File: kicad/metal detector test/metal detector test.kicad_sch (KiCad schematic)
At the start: 102 parts, among them J1 3.5mm audio jack TRS, Q1 PNP, Q2 NPN, SW0 SW_SPST, SW1 SW_SPST, SW10 SW_SPST, SW2 SW_SPST, SW3 SW_SPST, SW4 SW_SPST, SW5 SW_SPST, SW6 SW_SPST, SW7 SW_SPST, SW8 SW_SPST, U1 op amp (higher voltage), U10 3.3v lin reg, U11 lp filter, U12 op amp (lower voltage), U2 nucleo-32 uC module, U3 9v lin reg, U4 5v lin reg, U5 3.3v lin reg, U6 audio amp, U7 lp filter, U8 switch debounce, U9 5v lin reg

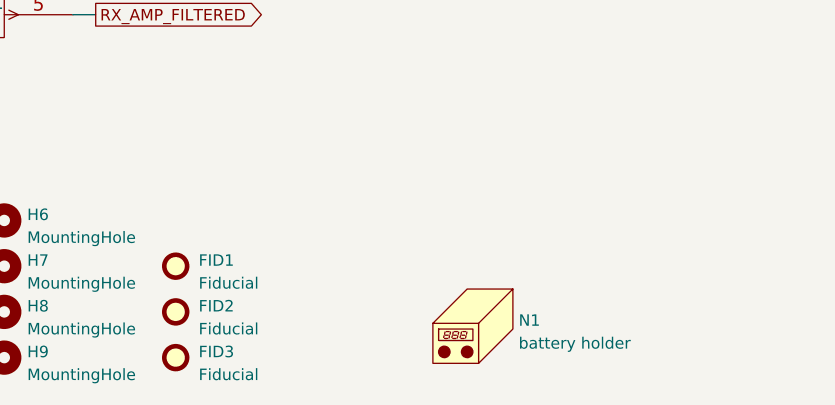
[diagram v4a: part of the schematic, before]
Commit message: Added a lot of fun silkscreen logos, and some other small tweaks
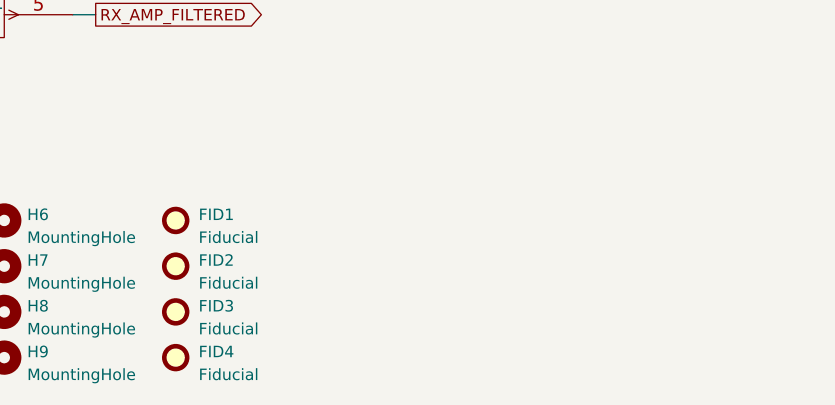
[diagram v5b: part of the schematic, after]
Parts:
- removed N1: battery holder, allen footprints:106990288_18650_x3_battery_holder, symbol Mechanical:Housing
- added FID4: Fiducial, Fiducial:Fiducial_0.5mm_Mask1.5mm, symbol Mechanical:Fiducial
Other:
- moved on the sheet: FID1, FID2, FID3
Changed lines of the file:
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@@
     )
   )
-  (symbol (lib_id "Mechanical:Fiducial") (at 124.46 194.31 0) (unit 1)
+  (symbol (lib_id "Mechanical:Fiducial") (at 124.46 189.23 0) (unit 1)
     (in_bom yes) (on_board yes) (dnp no) (fields_autoplaced)
-    (property "Reference" "FID3" (at 127 193.675 0)
+    (property "Reference" "FID3" (at 127 188.595 0)
       (effects (font (size 1.27 1.27)) (justify left))
     )
-    (property "Value" "Fiducial" (at 127 196.215 0)
+    (property "Value" "Fiducial" (at 127 191.135 0)
       (effects (font (size 1.27 1.27)) (justify left))
     )
-    (property "Footprint" "Fiducial:Fiducial_0.5mm_Mask1.5mm" (at 124.46 194.31 0)
+    (property "Footprint" "Fiducial:Fiducial_0.5mm_Mask1.5mm" (at 124.46 189.23 0)
       (effects (font (size 1.27 1.27)) hide)
     )
-    (property "Datasheet" "~" (at 124.46 194.31 0)
+    (property "Datasheet" "~" (at 124.46 189.23 0)
       (effects (font (size 1.27 1.27)) hide)
     )
-    (property "MPN" "" (at 124.46 194.31 0)
+    (property "MPN" "" (at 124.46 189.23 0)
       (effects (font (size 1.27 1.27)) hide)
     )
@@
     )
   )
-  (symbol (lib_id "Mechanical:Fiducial") (at 124.46 189.23 0) (unit 1)
+  (symbol (lib_id "Mechanical:Fiducial") (at 124.46 184.15 0) (unit 1)
     (in_bom yes) (on_board yes) (dnp no) (fields_autoplaced)
-    (property "Reference" "FID2" (at 127 188.595 0)
+    (property "Reference" "FID2" (at 127 183.515 0)
       (effects (font (size 1.27 1.27)) (justify left))
     )
-    (property "Value" "Fiducial" (at 127 191.135 0)
+    (property "Value" "Fiducial" (at 127 186.055 0)
       (effects (font (size 1.27 1.27)) (justify left))
     )
-    (property "Footprint" "Fiducial:Fiducial_0.5mm_Mask1.5mm" (at 124.46 189.23 0)
+    (property "Footprint" "Fiducial:Fiducial_0.5mm_Mask1.5mm" (at 124.46 184.15 0)
       (effects (font (size 1.27 1.27)) hide)
     )
-    (property "Datasheet" "~" (at 124.46 189.23 0)
+    (property "Datasheet" "~" (at 124.46 184.15 0)
       (effects (font (size 1.27 1.27)) hide)
     )
-    (property "MPN" "" (at 124.46 189.23 0)
+    (property "MPN" "" (at 124.46 184.15 0)
       (effects (font (size 1.27 1.27)) hide)
     )
@@
     )
   )
-  (symbol (lib_id "Mechanical:Fiducial") (at 124.46 184.15 0) (unit 1)
+  (symbol (lib_id "Mechanical:Fiducial") (at 124.46 179.07 0) (unit 1)
     (in_bom yes) (on_board yes) (dnp no) (fields_autoplaced)
-    (property "Reference" "FID1" (at 127 183.515 0)
+    (property "Reference" "FID1" (at 127 178.435 0)
       (effects (font (size 1.27 1.27)) (justify left))
     )
-    (property "Value" "Fiducial" (at 127 186.055 0)
+    (property "Value" "Fiducial" (at 127 180.975 0)
       (effects (font (size 1.27 1.27)) (justify left))
     )
-    (property "Footprint" "Fiducial:Fiducial_0.5mm_Mask1.5mm" (at 124.46 184.15 0)
+    (property "Footprint" "Fiducial:Fiducial_0.5mm_Mask1.5mm" (at 124.46 179.07 0)
       (effects (font (size 1.27 1.27)) hide)
     )
-    (property "Datasheet" "~" (at 124.46 184.15 0)
+    (property "Datasheet" "~" (at 124.46 179.07 0)
       (effects (font (size 1.27 1.27)) hide)
     )
-    (property "MPN" "" (at 124.46 184.15 0)
+    (property "MPN" "" (at 124.46 179.07 0)
       (effects (font (size 1.27 1.27)) hide)
     )
@@
     )
   )
+  (symbol (lib_id "Mechanical:Fiducial") (at 124.46 194.31 0) (unit 1)
+    (in_bom yes) (on_board yes) (dnp no) (fields_autoplaced)
+    (property "Reference" "FID4" (at 127 193.675 0)
+      (effects (font (size 1.27 1.27)) (justify left))
+    )
+    (property "Value" "Fiducial" (at 127 196.215 0)
+      (effects (font (size 1.27 1.27)) (justify left))
+    )
+    (property "Footprint" "Fiducial:Fiducial_0.5mm_Mask1.5mm" (at 124.46 194.31 0)
+      (effects (font (size 1.27 1.27)) hide)
+    )
+    (property "Datasheet" "~" (at 124.46 194.31 0)
+      (effects (font (size 1.27 1.27)) hide)
+    )
+    (property "MPN" "" (at 124.46 194.31 0)
+      (effects (font (size 1.27 1.27)) hide)
+    )
+    (instances
+      (project "metal detector test"
+        (path "/aac94249-970f-41d5-8c24-6bade512464d"
+          (reference "FID4") (unit 1)
+        )
+      )
+    )
+  )
   (symbol (lib_id "Switch:SW_SPST") (at 252.73 105.41 0) (unit 1)
     (in_bom yes) (on_board yes) (dnp no)
@@
         )
       )
-    )
-  )
-  (symbol (lib_id "Mechanical:Housing") (at 158.75 190.5 0) (unit 1)
-    (in_bom yes) (on_board yes) (dnp no) (fields_autoplaced)
-    (property "Reference" "N1" (at 162.56 190.1825 0)
-      (effects (font (size 1.27 1.27)) (justify left))
-    )
-    (property "Value" "battery holder" (at 162.56 192.7225 0)
-      (effects (font (size 1.27 1.27)) (justify left))
-    )
-    (property "Footprint" "allen footprints:106990288_18650_x3_battery_holder" (at 160.02 189.23 0)
-      (effects (font (size 1.27 1.27)) hide)
-    )
-    (property "Datasheet" "https://media.digikey.com/pdf/Data%20Sheets/Seeed%20Technology/106990288_Web.pdf" (at 160.02 189.23 0)
-      (effects (font (size 1.27 1.27)) hide)
-    )
-    (property "MPN" "106990288" (at 158.75 190.5 0)
-      (effects (font (size 1.27 1.27)) hide)
-    )
-    (instances
-      (project "metal detector test"
-        (path "/aac94249-970f-41d5-8c24-6bade512464d"
-          (reference "N1") (unit 1)
-        )
-      )

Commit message: Should be ready for fabrication
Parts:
- added C31: 3.3u, allen footprints:C_Polarized_0805_2012Metric_HandSolder_allen, symbol Device:C_Polarized_Small_US
- added JP6: SolderJumper_2_Open, Jumper:SolderJumper-2_P1.3mm_Open_Pad1.0x1.5mm, symbol Jumper:SolderJumper_2_Open
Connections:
- net GNDA: now also C31.2
- net at C3.1, DS1.2 (VCC), FB1.2: now also C31.1
- net at U2.27 (5V): now also JP6.1 (A); no longer JP3.1 (A)
- new net: JP3.1 (A), JP6.2 (B)
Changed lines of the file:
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@@
   (junction (at 85.09 156.21) (diameter 0) (color 0 0 0 0)
   )
+  (junction (at 256.54 43.18) (diameter 0) (color 0 0 0 0)
+  )
+  (junction (at 262.89 43.18) (diameter 0) (color 0 0 0 0)
+  )
   (junction (at 20.32 93.98) (diameter 0) (color 0 0 0 0)
   )
@@
   (junction (at 20.32 73.66) (diameter 0) (color 0 0 0 0)
   )
-  (junction (at 262.89 43.18) (diameter 0) (color 0 0 0 0)
-  )
   (junction (at 30.48 48.26) (diameter 0) (color 0 0 0 0)
   )
@@
     (stroke (width 0) (type default))
   )
-  (wire (pts (xy 262.89 29.21) (xy 262.89 43.18))
+  (wire (pts (xy 256.54 30.48) (xy 256.54 43.18))
     (stroke (width 0) (type default))
   )
@@
     (stroke (width 0) (type default))
   )
+  (wire (pts (xy 236.22 29.21) (xy 250.19 29.21))
+    (stroke (width 0) (type default))
+  )
   (wire (pts (xy 62.23 81.28) (xy 54.61 81.28))
     (stroke (width 0) (type default))
@@
     (stroke (width 0) (type default))
   )
+  (wire (pts (xy 262.89 43.18) (xy 265.43 43.18))
+    (stroke (width 0) (type default))
+  )
   (wire (pts (xy 97.79 102.87) (xy 109.22 102.87))
     (stroke (width 0) (type default))
@@
     (stroke (width 0) (type default))
   )
-  (wire (pts (xy 250.19 29.21) (xy 224.79 29.21))
-    (stroke (width 0) (type default))
-  )
   (wire (pts (xy 45.72 41.91) (xy 45.72 48.26))
     (stroke (width 0) (type default))
@@
     (stroke (width 0) (type default))
   )
+  (wire (pts (xy 262.89 31.75) (xy 262.89 43.18))
+    (stroke (width 0) (type default))
+  )
+  (wire (pts (xy 224.79 29.21) (xy 228.6 29.21))
+    (stroke (width 0) (type default))
+  )
   (wire (pts (xy 35.56 109.22) (xy 40.64 109.22))
     (stroke (width 0) (type default))
@@
     (stroke (width 0) (type default))
   )
-  (wire (pts (xy 262.89 43.18) (xy 265.43 43.18))
-    (stroke (width 0) (type default))
-  )
   (wire (pts (xy 176.53 69.85) (xy 248.92 69.85))
     (stroke (width 0) (type default))
@@
     )
   )
-  (symbol (lib_id "power:PWR_FLAG") (at 262.89 29.21 0) (unit 1)
+  (symbol (lib_id "power:PWR_FLAG") (at 256.54 30.48 0) (unit 1)
     (in_bom yes) (on_board yes) (dnp no) (fields_autoplaced)
-    (property "Reference" "#FLG01" (at 262.89 27.305 0)
+    (property "Reference" "#FLG01" (at 256.54 28.575 0)
       (effects (font (size 1.27 1.27)) hide)
     )
-    (property "Value" "PWR_FLAG" (at 262.89 25.4 0)
+    (property "Value" "PWR_FLAG" (at 256.54 26.67 0)
       (effects (font (size 1.27 1.27)))
     )
-    (property "Footprint" "" (at 262.89 29.21 0)
+    (property "Footprint" "" (at 256.54 30.48 0)
       (effects (font (size 1.27 1.27)) hide)
     )
-    (property "Datasheet" "~" (at 262.89 29.21 0)
+    (property "Datasheet" "~" (at 256.54 30.48 0)
       (effects (font (size 1.27 1.27)) hide)
     )
@@
     )
   )
+  (symbol (lib_id "Jumper:SolderJumper_2_Open") (at 232.41 29.21 0) (unit 1)
+    (in_bom yes) (on_board yes) (dnp no)
+    (property "Reference" "JP6" (at 232.41 26.67 0)
+      (effects (font (size 1.27 1.27)))
+    )
+    (property "Value" "SolderJumper_2_Open" (at 232.41 26.67 0)
+      (effects (font (size 1.27 1.27)) hide)
+    )
+    (property "Footprint" "Jumper:SolderJumper-2_P1.3mm_Open_Pad1.0x1.5mm" (at 232.41 29.21 0)
+      (effects (font (size 1.27 1.27)) hide)
+    )
+    (property "Datasheet" "~" (at 232.41 29.21 0)
+      (effects (font (size 1.27 1.27)) hide)
+    )
+    (pin "1")
+    (pin "2")
+    (instances
+      (project "metal detector test"
+        (path "/aac94249-970f-41d5-8c24-6bade512464d"
+          (reference "JP6") (unit 1)
+        )
+      )
+    )
+  )
+  (symbol (lib_id "power:GNDD") (at 262.89 26.67 180) (unit 1)
+    (in_bom yes) (on_board yes) (dnp no)
+    (property "Reference" "#PWR062" (at 262.89 20.32 0)
+      (effects (font (size 1.27 1.27)) hide)
+    )
+    (property "Value" "GNDD" (at 262.89 19.05 90)
+      (effects (font (size 1.27 1.27)) (justify left))
+    )
+    (property "Footprint" "" (at 262.89 26.67 0)
+      (effects (font (size 1.27 1.27)) hide)
+    )
+    (property "Datasheet" "" (at 262.89 26.67 0)
+      (effects (font (size 1.27 1.27)) hide)
+    )
+    (pin "1")
+    (instances
+      (project "metal detector test"
+        (path "/aac94249-970f-41d5-8c24-6bade512464d"
+          (reference "#PWR062") (unit 1)
+        )
+      )
+    )
+  )
   (symbol (lib_id "allen_opamp:OPA2320AID") (at 54.61 151.13 0) (mirror x) (unit 1)
     (in_bom yes) (on_board yes) (dnp no)
@@
         )
       )
+    )
+  )
+  (symbol (lib_id "Device:C_Polarized_Small_US") (at 262.89 29.21 180) (unit 1)
+    (in_bom yes) (on_board yes) (dnp no) (fields_autoplaced)
+    (property "Reference" "C31" (at 265.43 28.3718 0)
+      (effects (font (size 1.27 1.27)) (justify right))
+    )
+    (property "Value" "3.3u" (at 265.43 30.9118 0)
+      (effects (font (size 1.27 1.27)) (justify right))
+    )
+    (property "Footprint" "allen footprints:C_Polarized_0805_2012Metric_HandSolder_allen" (at 262.89 29.21 0)
+      (effects (font (size 1.27 1.27)) hide)
+    )
+    (property "Datasheet" "~" (at 262.89 29.21 0)
+      (effects (font (size 1.27 1.27)) hide)
+    )
+    (pin "1")
+    (pin "2")
+    (instances
+      (project "metal detector test"
+        (path "/aac94249-970f-41d5-8c24-6bade512464d"
+          (reference "C31") (unit 1)
+        )
+      )

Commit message: added a note about the 9v regulator's capacitor... turns out it can increase as large as needed
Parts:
- U3: cap note (none) -> COUT must be at least 22 μF to maintain stability. May be i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
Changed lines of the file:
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@@
+      (effects (font (size 1.27 1.27)) hide)
+    )
+    (property "cap note" "COUT must be at least 22 μF to maintain stability. May be increased without bound to maintain regulation during" (at 137.16 60.96 0)
       (effects (font (size 1.27 1.27)) hide)
     )
